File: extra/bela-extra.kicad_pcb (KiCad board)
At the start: 2 copper layers, 86 parts, among them P1 bbbp9, P10 GU128x64E-U100, P11 gui140x16j-7002, P12 digital_in, P13 digital_out, P14 ext_power, P2 bbbp8, P3 enc+btn1, P4 enc+btn2, P5 MTA-156-4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

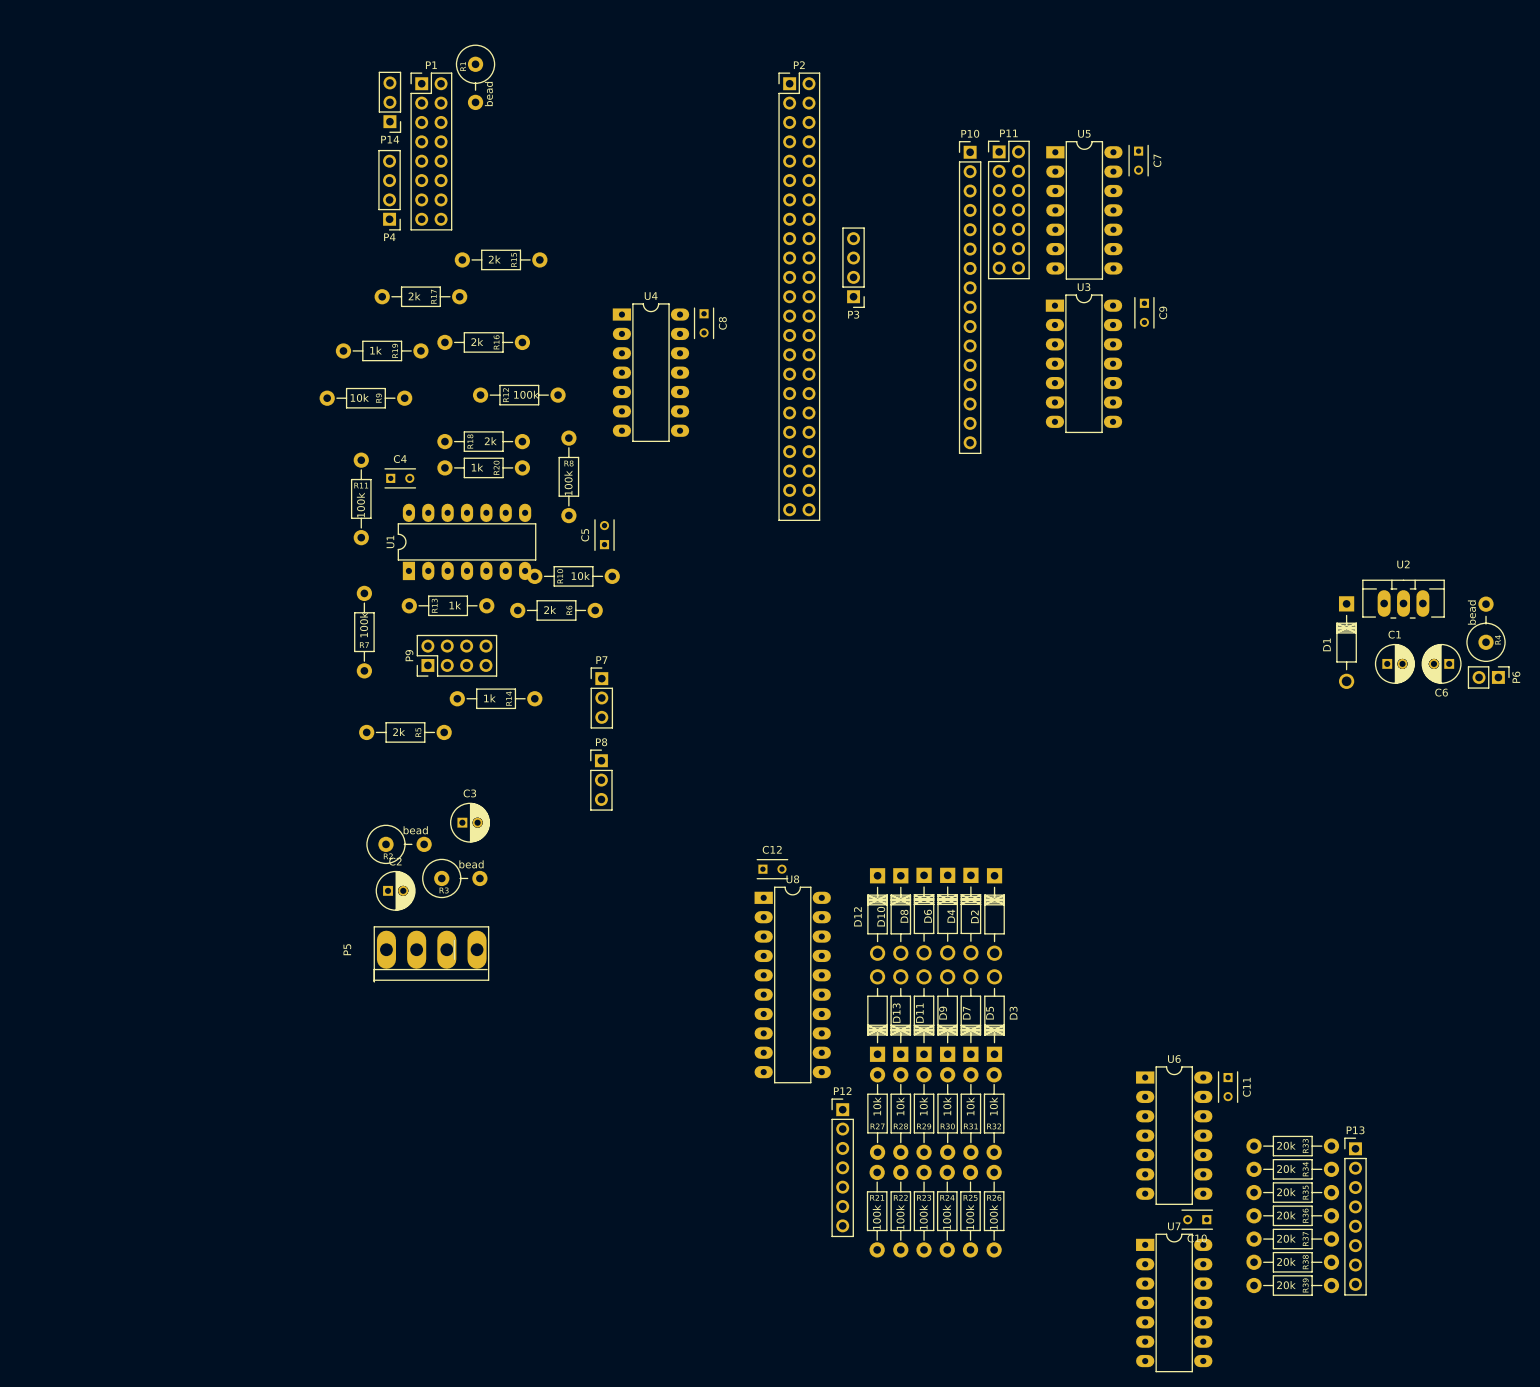
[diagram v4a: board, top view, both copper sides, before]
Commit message: more layout, gonna split into 2 boards
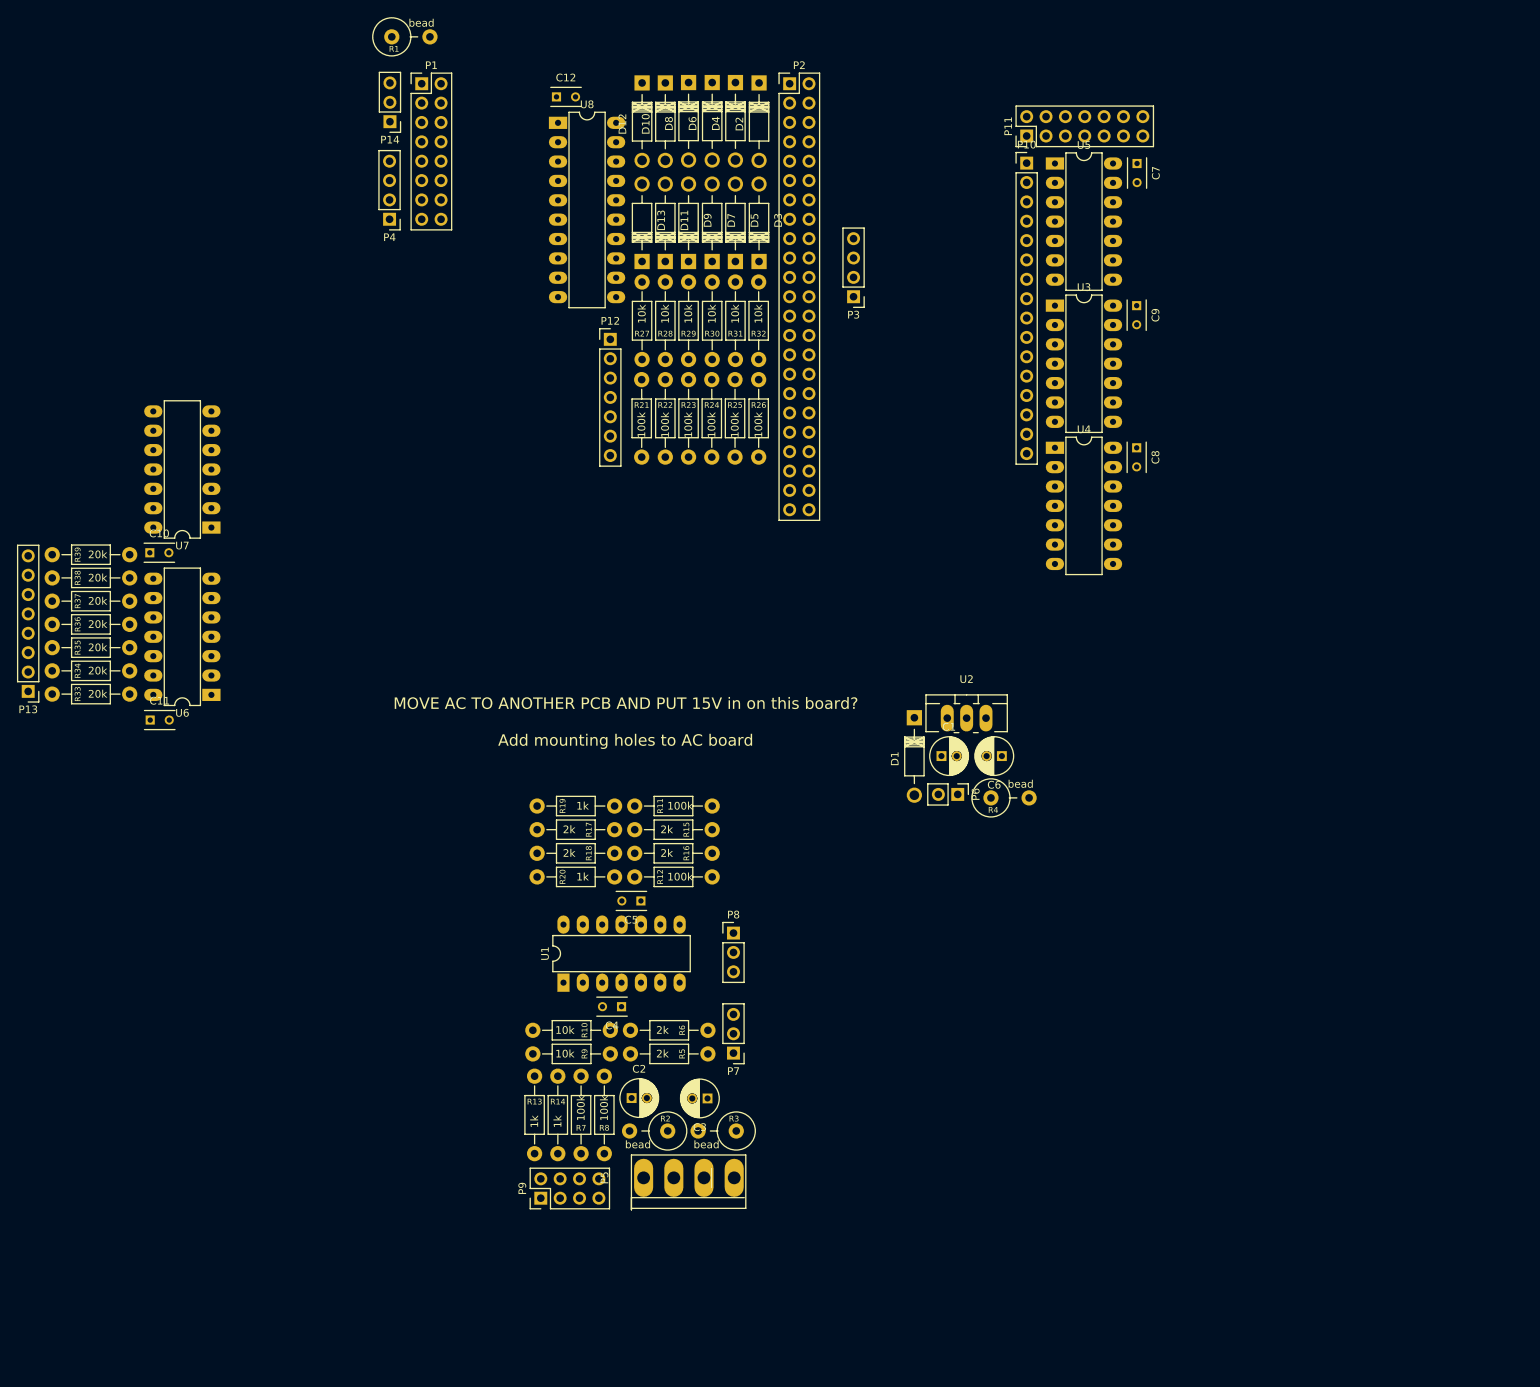
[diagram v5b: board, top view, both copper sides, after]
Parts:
- moved P13 184.1 mm to (-26.2, 105.1), turned to 180 degrees
- moved R39 175.9 mm to (-12.9, 87.2), turned to 180 degrees
- moved R38 172.6 mm to (-12.9, 90.2), turned to 180 degrees
- moved R37 169.6 mm to (-12.9, 93.3), turned to 180 degrees
- moved R36 166.6 mm to (-12.9, 96.3), turned to 180 degrees
- moved C10 163.9 mm to (-10.3, 86.9), turned to 0 degrees
- moved R35 163.9 mm to (-12.9, 99.4), turned to 180 degrees
- moved R34 161.3 mm to (-12.9, 102.4), turned to 180 degrees
- moved R33 158.9 mm to (-12.9, 105.5), turned to 180 degrees
- moved U7 154.4 mm to (-2.18, 83.6), turned to 180 degrees
- moved C11 148.9 mm to (-10.2, 108.9), turned to 0 degrees
- moved U6 132.4 mm to (-2.18, 105.6), turned to 180 degrees
- moved D11 108.5 mm to (57.4, 48.7)
- moved D13 108.5 mm to (54.3, 48.7)
- moved D3 108.5 mm to (69.6, 48.7)
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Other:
- board text added: "MOVE AC TO ANOTHER PCB AND PUT 15V in on this board? Add mounting holes to AC board"

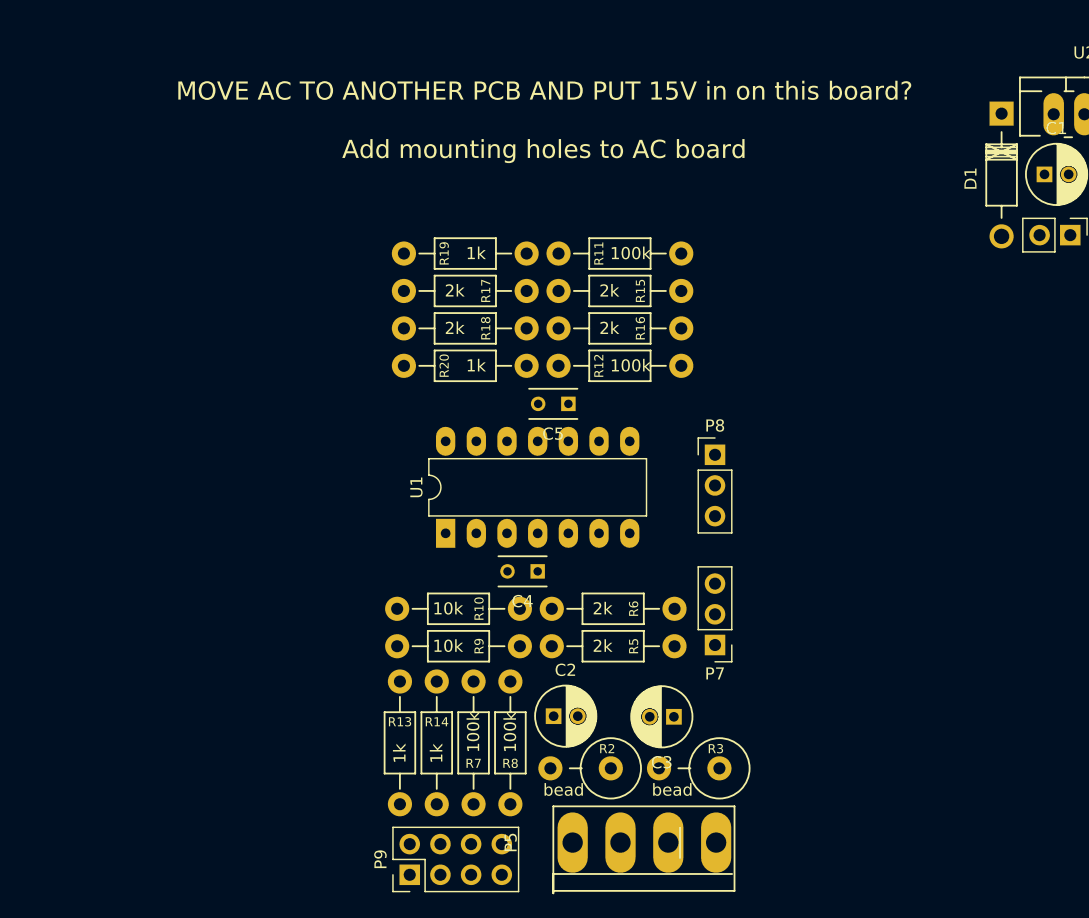
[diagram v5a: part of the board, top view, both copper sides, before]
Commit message: removed ac from extra, added power connection for 15
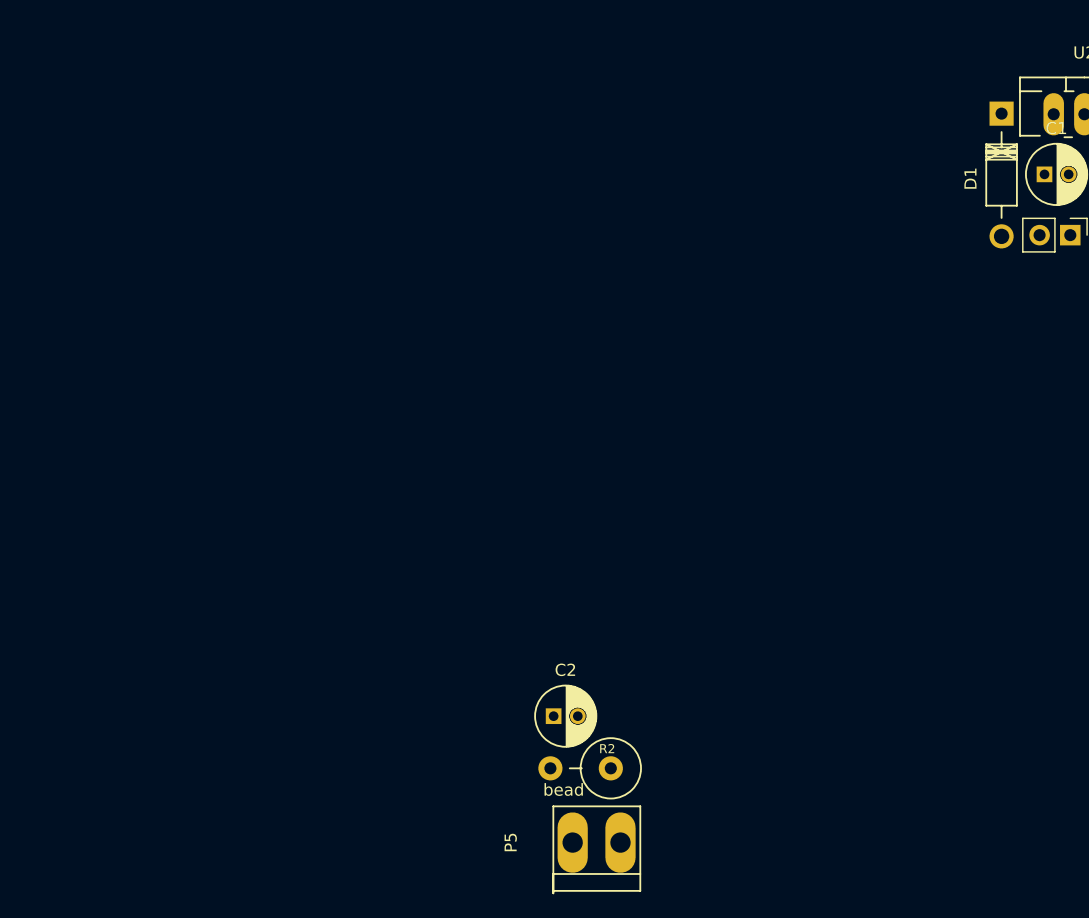
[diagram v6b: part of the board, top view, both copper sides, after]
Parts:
- removed C3: 10uF, Capacitors_ThroughHole:C_Radial_D5_L11_P2
- removed C4, C5: 10n, Capacitors_ThroughHole:C_Rect_L4_W2.5_P2.5
- removed P7: belaaudioout, Pin_Headers:Pin_Header_Straight_1x03_Pitch2.54mm
- removed P8: belaaudioin, Pin_Headers:Pin_Header_Straight_1x03_Pitch2.54mm
- removed P9: mod_ac-io, Pin_Headers:Pin_Header_Straight_2x04_Pitch2.54mm
- removed R10, R9: 10k, xnorman:Resistor_Horizontal_RM10mm-xnorman
- removed R11, R12, R7, R8: 100k, xnorman:Resistor_Horizontal_RM10mm-xnorman
- removed R13, R14, R19, R20: 1k, xnorman:Resistor_Horizontal_RM10mm-xnorman
- removed R15, R16, R17, R18, R5, R6: 2k, xnorman:Resistor_Horizontal_RM10mm-xnorman
- removed R3: bead, xnorman:Resistor_Vertical_RM5mm-xnor
- removed U1: TL074, Housings_DIP:DIP-14_W7.62mm_LongPads
- P5: value MTA-156-4 -> MTA-156-2; footprint mta-156:MTA-156-4 -> mta-156:MTA-156-2
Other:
- board text removed: "MOVE AC TO ANOTHER PCB AND PUT 15V in on this board? Add mounting holes to AC board"

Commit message: fixed up labeling
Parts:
- P11: value gui140x16j-7002 -> gu140x16j-7002
- P5: value MTA-156-2 -> power_in
- P6: value bela_power -> bbb_power; footprint Pin_Headers:Pin_Header_Straight_1x02_Pitch2.54mm -> mta-156:MTA-156-2
- U2: value 7805-xnor -> 7805
- U8: value 74LS245-xnor -> 74LS245
- moved P5 153.6 mm to (72.2, 16.4)
- moved R2 144.2 mm to (59.0, 18.6), turned to 270 degrees
- moved C2 139.9 mm to (64.8, 19.1), turned to 90 degrees
- moved R4 120.5 mm to (38.5, 17.1)
- moved P6 120.0 mm to (31.3, 17.3)
- moved C1 103.6 mm to (46.7, 21.2)
- moved C6 103.4 mm to (55.4, 21.0)
- moved U2 103.4 mm to (50.5, 16.2)
- moved P11 103.1 mm to (23.7, 96.0), turned to 180 degrees
- moved C7 102.6 mm to (27.3, 81.5), turned to 0 degrees
- moved D1 100.6 mm to (43.0, 19.7)
- moved U5 98.8 mm to (27.3, 92.3), turned to 90 degrees
- moved P10 98.1 mm to (27.3, 96.0), turned to 90 degrees
- moved C9 78.0 mm to (46.0, 81.6), turned to 0 degrees
- moved U3 73.0 mm to (46.0, 92.3), turned to 90 degrees
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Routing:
- added copper zone on B.Cu, net GND
- added copper zone on F.Cu, net GND
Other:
- board outline added: 63 x 85.3 mm
- board text added: "+"
- board text added: "15v"
- board text added: "3v3"
- board text added: "5v"
- board text added: "gnd"

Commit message: all layed out
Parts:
- moved P12 36.6 mm to (42.8, 57.1), turned to 90 degrees
- moved C11 32.9 mm to (62.0, 76.1)
- moved U6 32.6 mm to (69.6, 73.1)
- moved D3 31.0 mm to (41.6, 25.0), turned to 180 degrees
- moved D5 27.0 mm to (41.6, 27.8), turned to 180 degrees
- moved D7 23.1 mm to (41.6, 30.7), turned to 180 degrees
- moved C12 21.7 mm to (62.0, 23.7)
- moved U7 21.5 mm to (39.6, 59.5)
- moved C10 21.5 mm to (32.0, 62.8)
- moved U8 21.5 mm to (62.1, 27.3)
- moved D9 19.4 mm to (41.6, 33.5), turned to 180 degrees
- moved P11 19.4 mm to (42.8, 92.6), turned to 90 degrees
- moved D11 15.9 mm to (41.6, 36.4), turned to 180 degrees
- moved R28 14.9 mm to (45.8, 42.0)
- moved R29 14.9 mm to (48.9, 42.0)
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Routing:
- net 5v: track 0.00 -> 203.8 mm, vias 0 -> 1
- net GND: track 0.00 -> 88.1 mm, vias 0 -> 13
- net beladigout7: track 0.00 -> 72.5 mm
- net vfdD7: track 0.00 -> 70.1 mm
- net 3.3v: track 0.00 -> 70.1 mm
- net bb-vfd-RD+RW: track 0.00 -> 66.9 mm
- net bb-vfdE: track 0.00 -> 63.1 mm
- net bb-vfd-WR+RS: track 0.00 -> 60.5 mm, vias 0 -> 2
- net bb-vfdCS2: track 0.00 -> 52.5 mm
- net vfdE: track 0.00 -> 49.0 mm
- net vfdCS2: track 0.00 -> 48.9 mm
- net bb-vfdCS1: track 0.00 -> 46.8 mm
- net beladigout6: track 0.00 -> 44.9 mm
- net moddigout2: track 0.00 -> 37.4 mm
- net moddigout1: track 0.00 -> 37.2 mm
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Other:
- board text added: "http://x37v.info"
- board text added: "modular digital <-> bela + VFD"
- board text added: "xnor 1/17"
